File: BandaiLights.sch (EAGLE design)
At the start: 16 parts, among them Q1 FAN5333B, U1 AAAA-BATTERY, U2 AAAA-BATTERY

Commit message: Revised PCB: - Revised LED layout to avoid having to rework the interior of the Falcon to fit all 6 LEDs - Revised silk screen to make it more readable. - Added GK (geek kids logo).
Added license.
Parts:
- added TP1, TP2, TP3, TP4: TPB1,27, testpad:TPB1,27
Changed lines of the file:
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@@
 <?xml version="1.0" encoding="utf-8"?>
 <!DOCTYPE eagle SYSTEM "eagle.dtd">
-<eagle version="7.0.0">
+<eagle version="7.4.0">
 <drawing>
 <settings>
@@
 <part name="U$4" library="SAVMakerI" deviceset="SPARKFUN_OSHW-LOGO" device="M"/>
 <part name="L1" library="inductors" deviceset="LQHXXSN" device="LQH55DN" value="10uH-SRN3015-100M"/>
+<part name="TP1" library="testpad" deviceset="TP" device="B1,27"/>
+<part name="TP2" library="testpad" deviceset="TP" device="B1,27"/>
+<part name="TP3" library="testpad" deviceset="TP" device="B1,27"/>
+<part name="TP4" library="testpad" deviceset="TP" device="B1,27"/>
 </parts>
 <sheets>
@@
 <attribute name="VALUE" x="82.55" y="129.159" size="1.778" layer="96"/>
 </instance>
+<instance part="TP1" gate="G$1" x="33.02" y="33.02"/>
+<instance part="TP2" gate="G$1" x="38.1" y="33.02"/>
+<instance part="TP3" gate="G$1" x="43.18" y="33.02"/>
+<instance part="TP4" gate="G$1" x="48.26" y="33.02"/>
 </instances>
 <busses>

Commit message: Release Rev B, untested.
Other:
- note added: "B"
- note removed: "A"
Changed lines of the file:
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@@
 <?xml version="1.0" encoding="utf-8"?>
 <!DOCTYPE eagle SYSTEM "eagle.dtd">
-<eagle version="7.4.0">
+<eagle version="7.0.0">
 <drawing>
 <settings>
@@
 <plain>
 <text x="76.2" y="96.52" size="1.778" layer="97">FAN5333B</text>
-<text x="255.778" y="4.064" size="3.81" layer="97">A</text>
+<text x="255.778" y="4.064" size="3.81" layer="97">B</text>
 <text x="199.898" y="23.622" size="2.54" layer="97" ratio="10">Model LED lights
 Falcon LEDs</text>

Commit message: Updated schematics.
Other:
- note added: "Model LED lights Falcon LEDs - By: F. Malpartida & GeekKids"
- note removed: "Model LED lights Falcon LEDs"
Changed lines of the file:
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@@
 <?xml version="1.0" encoding="utf-8"?>
 <!DOCTYPE eagle SYSTEM "eagle.dtd">
-<eagle version="7.0.0">
+<eagle version="7.6.0">
 <drawing>
 <settings>
@@
 <text x="76.2" y="96.52" size="1.778" layer="97">FAN5333B</text>
 <text x="255.778" y="4.064" size="3.81" layer="97">B</text>
-<text x="199.898" y="23.622" size="2.54" layer="97" ratio="10">Model LED lights
-Falcon LEDs</text>
+<text x="166.878" y="23.622" size="2.54" layer="97" ratio="10">Model LED lights
+Falcon LEDs - By: F. Malpartida &amp; GeekKids</text>
 <text x="83.82" y="154.94" size="5.08" layer="97" ratio="10">Battery powered LED lights</text>
 <text x="5.08" y="10.16" size="2.54" layer="97">Released under the CERN Open Hardware Licence v1.2 </text>

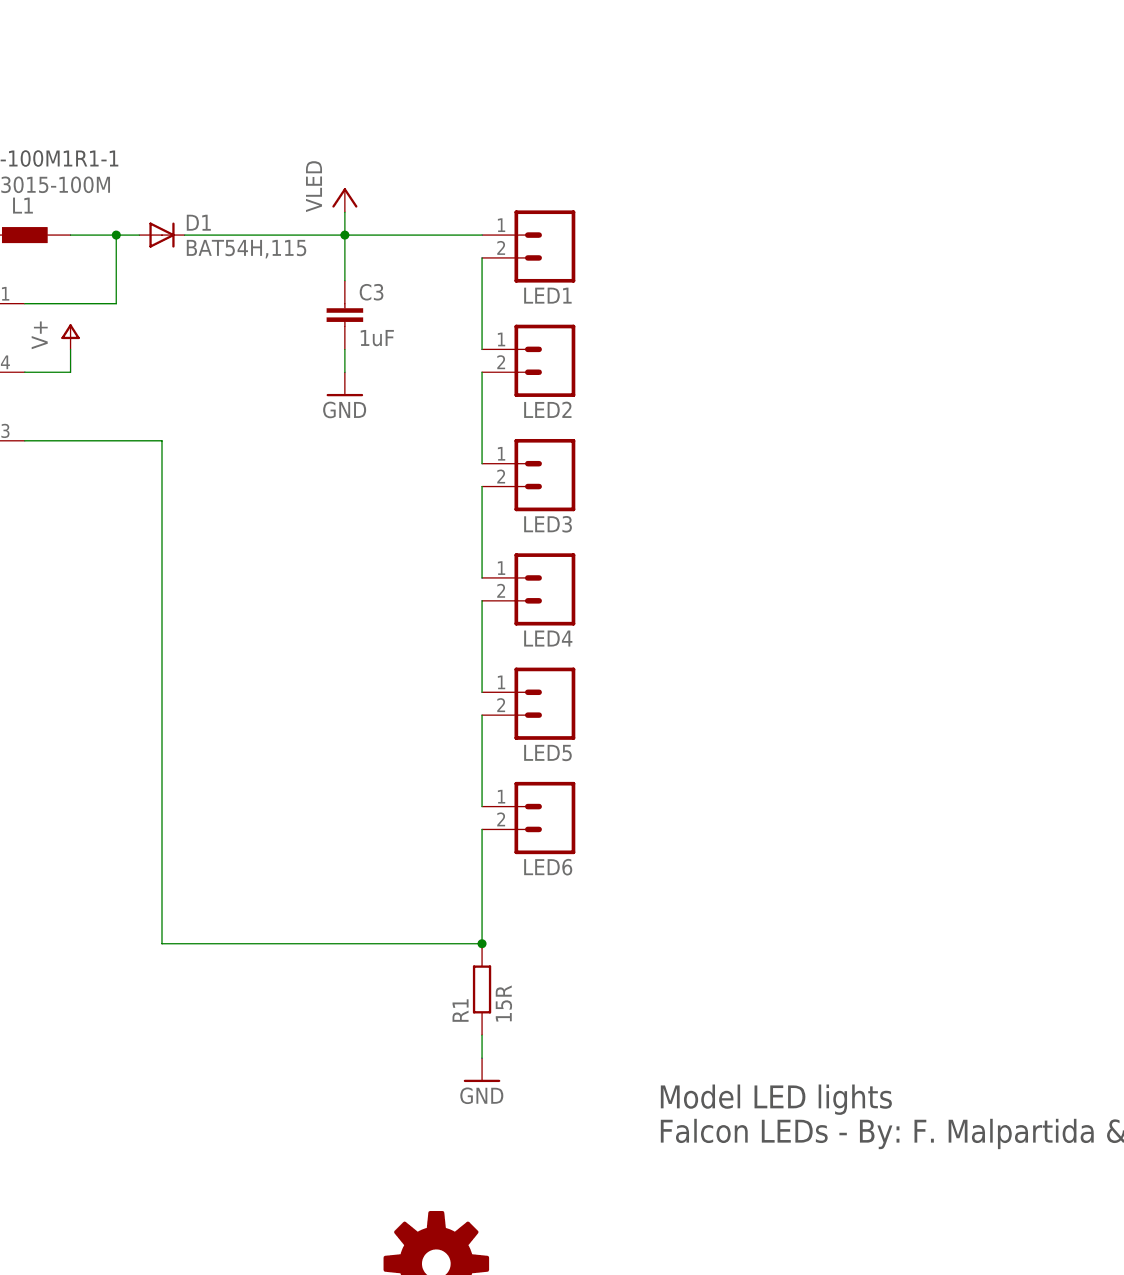
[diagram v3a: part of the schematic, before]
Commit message: Updated LED setup to be in parallel.
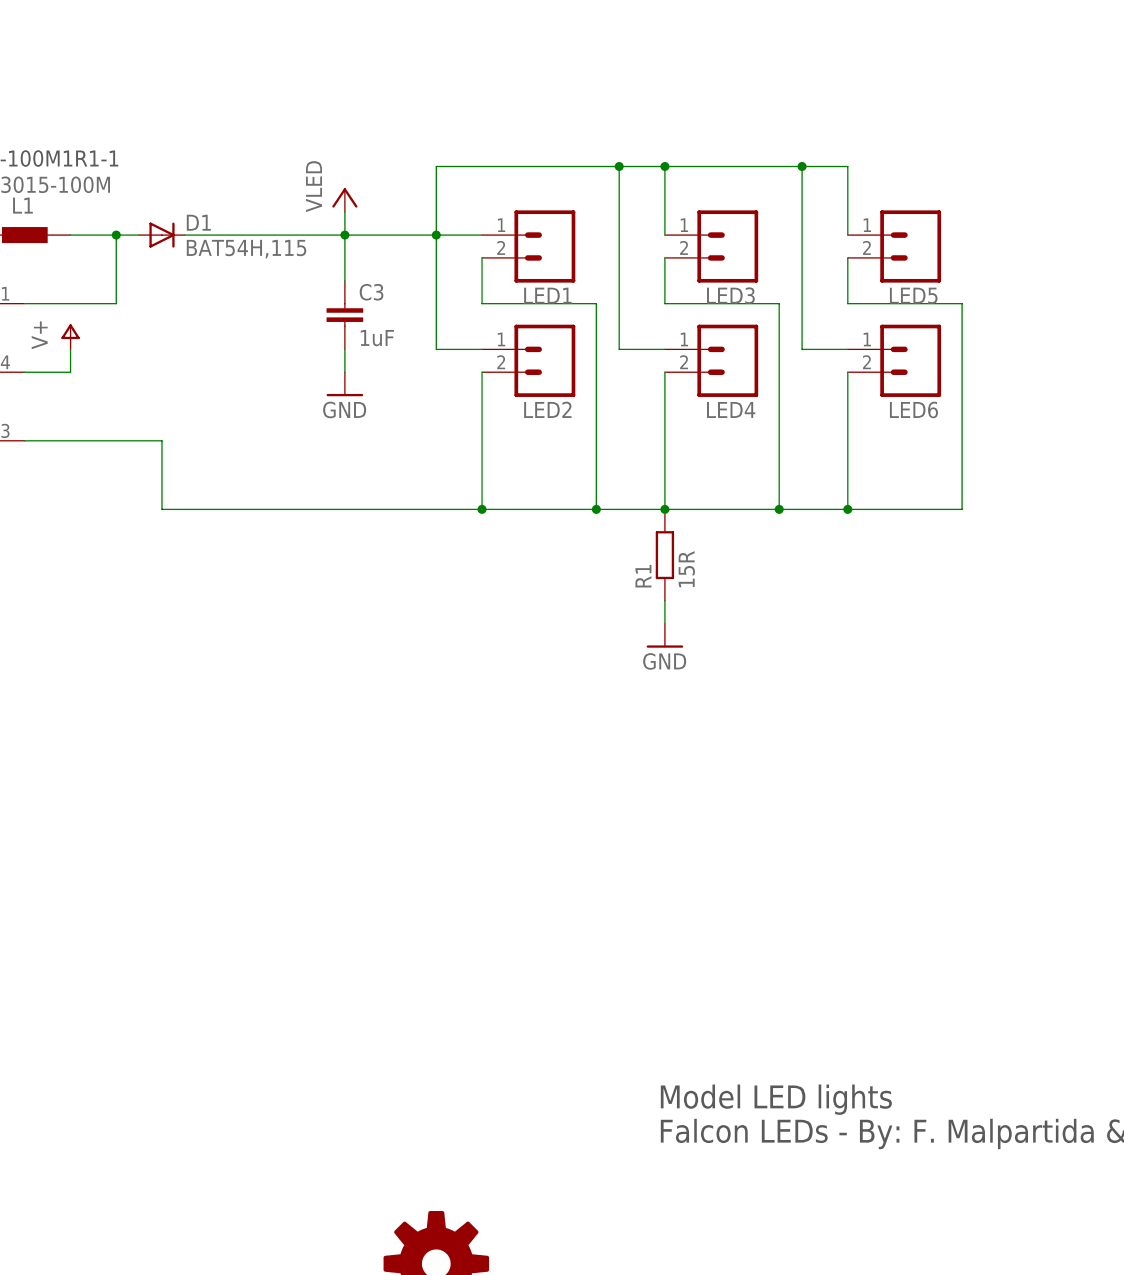
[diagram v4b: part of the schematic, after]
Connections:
- removed net N$1: LED1.2, LED2.1
- removed net N$2: LED2.2, LED3.1
- removed net N$3: LED3.2, LED4.1
- removed net N$4: LED4.2, LED5.1
- removed net N$6: LED5.2, LED6.1
- net FB: now also LED1.2, LED2.2, LED3.2, LED4.2, LED5.2
- net VCC: now also LED2.1, LED3.1, LED4.1, LED5.1, LED6.1
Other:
- moved on the sheet: LED3, LED4, LED5, LED6, R1
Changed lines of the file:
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@@
 <text x="5.08" y="10.16" size="2.54" layer="97">Released under the CERN Open Hardware Licence v1.2 </text>
 <text x="5.08" y="5.08" size="2.54" layer="97">http://www.ohwr.org/attachments/2388/cern_ohl_v_1_2.txt</text>
-<text x="170.18" y="116.84" size="1.778" layer="98">Jumpers between LED connectors for those
+<text x="170.18" y="134.62" size="1.778" layer="98">Jumpers between LED connectors for those
 that are not being used.</text>
 <text x="81.28" y="132.08" size="1.778" layer="97">VLCF5020T-100M1R1-1</text>
@@
 <instance part="P+3" gate="1" x="60.96" y="129.54"/>
 <instance part="GND6" gate="1" x="60.96" y="93.98"/>
-<instance part="R1" gate="G$1" x="147.32" y="40.64" rot="R90"/>
-<instance part="GND8" gate="1" x="147.32" y="30.48"/>
+<instance part="R1" gate="G$1" x="167.64" y="88.9" rot="R90"/>
+<instance part="GND8" gate="1" x="167.64" y="78.74"/>
 <instance part="Q1" gate="G$1" x="78.74" y="109.22"/>
 <instance part="GND7" gate="1" x="68.58" y="93.98"/>
@@
 <instance part="LED1" gate="G$1" x="154.94" y="124.46" rot="R180"/>
 <instance part="LED2" gate="G$1" x="154.94" y="111.76" rot="R180"/>
-<instance part="LED3" gate="G$1" x="154.94" y="99.06" rot="R180"/>
-<instance part="LED4" gate="G$1" x="154.94" y="86.36" rot="R180"/>
-<instance part="LED5" gate="G$1" x="154.94" y="73.66" rot="R180"/>
-<instance part="LED6" gate="G$1" x="154.94" y="60.96" rot="R180"/>
+<instance part="LED3" gate="G$1" x="175.26" y="124.46" rot="R180"/>
+<instance part="LED4" gate="G$1" x="175.26" y="111.76" rot="R180"/>
+<instance part="LED5" gate="G$1" x="195.58" y="124.46" rot="R180"/>
+<instance part="LED6" gate="G$1" x="195.58" y="111.76" rot="R180"/>
 <instance part="U1" gate="G$1" x="35.56" y="111.76" smashed="yes" rot="R90">
 <attribute name="NAME" x="32.385" y="109.22" size="1.778" layer="95" rot="R90"/>
@@
 <pinref part="R1" gate="G$1" pin="1"/>
 <pinref part="GND8" gate="1" pin="GND"/>
-<wire x1="147.32" y1="33.02" x2="147.32" y2="35.56" width="0.1524" layer="91"/>
+<wire x1="167.64" y1="81.28" x2="167.64" y2="83.82" width="0.1524" layer="91"/>
 </segment>
 <segment>
@@
 <pinref part="R1" gate="G$1" pin="2"/>
 <pinref part="Q1" gate="G$1" pin="FB"/>
-<wire x1="147.32" y1="45.72" x2="111.76" y2="45.72" width="0.1524" layer="91"/>
+<wire x1="167.64" y1="93.98" x2="160.02" y2="93.98" width="0.1524" layer="91"/>
+<wire x1="160.02" y1="93.98" x2="147.32" y2="93.98" width="0.1524" layer="91"/>
+<wire x1="147.32" y1="93.98" x2="111.76" y2="93.98" width="0.1524" layer="91"/>
 <wire x1="96.52" y1="101.6" x2="111.76" y2="101.6" width="0.1524" layer="91"/>
-<wire x1="111.76" y1="101.6" x2="111.76" y2="45.72" width="0.1524" layer="91"/>
+<wire x1="111.76" y1="101.6" x2="111.76" y2="93.98" width="0.1524" layer="91"/>
+<pinref part="LED2" gate="G$1" pin="2"/>
+<wire x1="147.32" y1="109.22" x2="147.32" y2="93.98" width="0.1524" layer="91"/>
+<junction x="147.32" y="93.98"/>
+<pinref part="LED4" gate="G$1" pin="2"/>
+<wire x1="167.64" y1="109.22" x2="167.64" y2="93.98" width="0.1524" layer="91"/>
+<junction x="167.64" y="93.98"/>
 <pinref part="LED6" gate="G$1" pin="2"/>
-<wire x1="147.32" y1="58.42" x2="147.32" y2="45.72" width="0.1524" layer="91"/>
-<junction x="147.32" y="45.72"/>
+<wire x1="187.96" y1="109.22" x2="187.96" y2="93.98" width="0.1524" layer="91"/>
+<wire x1="187.96" y1="93.98" x2="180.34" y2="93.98" width="0.1524" layer="91"/>
+<pinref part="LED1" gate="G$1" pin="2"/>
+<wire x1="180.34" y1="93.98" x2="167.64" y2="93.98" width="0.1524" layer="91"/>
+<wire x1="147.32" y1="121.92" x2="147.32" y2="116.84" width="0.1524" layer="91"/>
+<wire x1="147.32" y1="116.84" x2="160.02" y2="116.84" width="0.1524" layer="91"/>
+<wire x1="160.02" y1="116.84" x2="160.02" y2="93.98" width="0.1524" layer="91"/>
+<junction x="160.02" y="93.98"/>
+<wire x1="167.64" y1="121.92" x2="167.64" y2="116.84" width="0.1524" layer="91"/>
+<wire x1="167.64" y1="116.84" x2="180.34" y2="116.84" width="0.1524" layer="91"/>
+<wire x1="180.34" y1="116.84" x2="180.34" y2="93.98" width="0.1524" layer="91"/>
+<junction x="180.34" y="93.98"/>
+<wire x1="187.96" y1="93.98" x2="200.66" y2="93.98" width="0.1524" layer="91"/>
+<wire x1="200.66" y1="93.98" x2="200.66" y2="116.84" width="0.1524" layer="91"/>
+<junction x="187.96" y="93.98"/>
+<pinref part="LED5" gate="G$1" pin="2"/>
+<wire x1="200.66" y1="116.84" x2="187.96" y2="116.84" width="0.1524" layer="91"/>
+<wire x1="187.96" y1="116.84" x2="187.96" y2="121.92" width="0.1524" layer="91"/>
+<pinref part="LED3" gate="G$1" pin="2"/>
 </segment>
 </net>
@@
 <wire x1="132.08" y1="127" x2="132.08" y2="124.46" width="0.1524" layer="91"/>
 <pinref part="LED1" gate="G$1" pin="1"/>
-<wire x1="132.08" y1="124.46" x2="147.32" y2="124.46" width="0.1524" layer="91"/>
+<wire x1="132.08" y1="124.46" x2="142.24" y2="124.46" width="0.1524" layer="91"/>
+<pinref part="LED3" gate="G$1" pin="1"/>
+<wire x1="142.24" y1="124.46" x2="147.32" y2="124.46" width="0.1524" layer="91"/>
+<wire x1="167.64" y1="124.46" x2="167.64" y2="132.08" width="0.1524" layer="91"/>
+<wire x1="167.64" y1="132.08" x2="162.56" y2="132.08" width="0.1524" layer="91"/>
+<wire x1="162.56" y1="132.08" x2="142.24" y2="132.08" width="0.1524" layer="91"/>
+<wire x1="142.24" y1="132.08" x2="142.24" y2="124.46" width="0.1524" layer="91"/>
+<junction x="142.24" y="124.46"/>
+<pinref part="LED5" gate="G$1" pin="1"/>
+<wire x1="187.96" y1="124.46" x2="187.96" y2="132.08" width="0.1524" layer="91"/>
+<wire x1="187.96" y1="132.08" x2="182.88" y2="132.08" width="0.1524" layer="91"/>
+<junction x="167.64" y="132.08"/>
+<wire x1="182.88" y1="132.08" x2="167.64" y2="132.08" width="0.1524" layer="91"/>
+<wire x1="147.32" y1="111.76" x2="142.24" y2="111.76" width="0.1524" layer="91"/>
+<wire x1="142.24" y1="111.76" x2="142.24" y2="124.46" width="0.1524" layer="91"/>
+<pinref part="LED4" gate="G$1" pin="1"/>
+<wire x1="167.64" y1="111.76" x2="162.56" y2="111.76" width="0.1524" layer="91"/>
+<wire x1="162.56" y1="111.76" x2="162.56" y2="132.08" width="0.1524" layer="91"/>
+<junction x="162.56" y="132.08"/>
+<pinref part="LED6" gate="G$1" pin="1"/>
+<wire x1="187.96" y1="111.76" x2="182.88" y2="111.76" width="0.1524" layer="91"/>
+<wire x1="182.88" y1="111.76" x2="182.88" y2="132.08" width="0.1524" layer="91"/>
+<junction x="182.88" y="132.08"/>
+<pinref part="LED2" gate="G$1" pin="1"/>
 </segment>
 </net>
-<net name="N$1" class="0">
-<segment>
-<pinref part="LED1" gate="G$1" pin="2"/>
-<pinref part="LED2" gate="G$1" pin="1"/>
-<wire x1="147.32" y1="121.92" x2="147.32" y2="111.76" width="0.1524" layer="91"/>
-</segment>
-</net>
-<net name="N$2" class="0">
-<segment>
-<pinref part="LED2" gate="G$1" pin="2"/>
-<pinref part="LED3" gate="G$1" pin="1"/>
-<wire x1="147.32" y1="109.22" x2="147.32" y2="99.06" width="0.1524" layer="91"/>
-</segment>
-</net>
-<net name="N$3" class="0">
-<segment>
-<pinref part="LED3" gate="G$1" pin="2"/>
-<pinref part="LED4" gate="G$1" pin="1"/>
-<wire x1="147.32" y1="96.52" x2="147.32" y2="86.36" width="0.1524" layer="91"/>
-</segment>
-</net>
-<net name="N$4" class="0">
-<segment>
-<pinref part="LED4" gate="G$1" pin="2"/>
-<pinref part="LED5" gate="G$1" pin="1"/>
-<wire x1="147.32" y1="83.82" x2="147.32" y2="73.66" width="0.1524" layer="91"/>
-</segment>
-</net>
-<net name="N$6" class="0">
-<segment>
-<pinref part="LED5" gate="G$1" pin="2"/>
-<pinref part="LED6" gate="G$1" pin="1"/>
-<wire x1="147.32" y1="71.12" x2="147.32" y2="60.96" width="0.1524" layer="91"/>
-</segment>
-</net>
